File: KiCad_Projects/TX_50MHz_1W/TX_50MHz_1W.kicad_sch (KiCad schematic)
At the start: 7 parts

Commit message: Sync TX and RX schematic connectivity with target netlists
Repair the electrical connectivity of both single-sheet schematics so that a
netlist exported with kicad-cli 10 matches the connectivity described by
TX_50MHz_1W.net / RX_50MHz_SDR.net and the TX/RX schematic blueprints.

TX_50MHz_1W.kicad_sch
- Split the I2C bus: two coincident global labels (I2C_SDA + I2C_SCL on the
  same point at ESP32 IO11) had merged SDA and SCL into one net that also
  dragged in the BGS12PL6 CTRL/RF2 pins and the SPF5043Z RF input.  SDA now
  lands on IO8 and SCL on IO9 only.
- Removed the wire chain that shorted ESP32 IO8..IO11 together.
- 3V3 rail: every IC VDD sat on an island with just its decoupling cap.
  Labelled U1/U2/U3/U6/U7/U8 supply pins onto 3V3, and grounded the six
  decoupling caps that had a floating leg.
- PA drain: dropped the junction that tied Q1 drain onto the Si5351A CLK1
  wire.  TX_PATH is now Q1 drain + BGS12PL6 RF1 + RFC L2, with V_BATT feeding
  the drain through L2 as the blueprint specifies.  TELEM_LO (CLK1 -> LT5560
  LO+) is carried by labels instead of a wire crossing the drain node.
- Telemetry RX chain: BGS12PL6 RF2 -> SPF5043Z RFin (RX_PATH) and SPF5043Z
  RFout -> LT5560 IN+ (LNA_OUT) were open (wires stopped short of the pin).
- ADC: the 10.7MHz filter output ran to a wire end 4.5mm away from the MCU.
  FL1 OUT and ESP32 IO10 are now on ADC_IN.
- T/R control: BGS12PL6 CTRL and ESP32 IO11 are now on TR_SW_CTRL.
- Output LPF: the four shunt caps had GND on their series legs, which shorted
  the BGS12PL6 antenna port and the whole filter to ground.  GND moved to the
  free leg of each cap and the series path is now a proper 4C/3L low-pass
  from the switch ANT pin to the SMA.

RX_50MHz_SDR.kicad_sch
- Si5351A VDD was held on 3V3 only by a label sitting mid-wire; moved it to
  the open end of the stub, matching the SCL/SDA stubs next to it.
- Removed the duplicate XTAL_A label (two identical labels on one point
  cancel each other out in KiCad, so th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
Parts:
- removed FL?: 10.7MHz_Filter, symbol Kraft6M:10.7MHz_Filter
- removed Q?: 1W PA, symbol RD01MUS2
- removed U?: SPF5043Z, symbol Kraft6M:SPF5043Z
- removed U?: LT5560, symbol Kraft6M:LT5560
- removed U?: ESP32-S3, symbol ESP32-S3-WROOM-1
- removed U?: BGS12PL6, symbol Kraft6M:BGS12PL6
- removed U?: Si5351A, symbol Si5351A
- added C1: 10nF, Capacitor_SMD:C_0603_1608Metric, symbol Kraft6M:C_10nF_0603
- added C10, C11, C6, C7, C8, C9: 0.1uF, Capacitor_SMD:C_0603_1608Metric, symbol Kraft6M:C_0.1uF_0603
- added C2, C5: 120pF, Capacitor_SMD:C_0805_2012Metric, symbol Kraft6M:C_120pF_0805
- added C3, C4: 220pF, Capacitor_SMD:C_0805_2012Metric, symbol Kraft6M:C_220pF_0805
- added FL1: 10.7MHz Murata SFE, Filter:Ceramic_Filter_Murata_SFE, symbol Kraft6M:10.7MHz_Filter
- added J1: AIL Stick, Connector_JST:JST_XH_B3B-XH-A_1x03_P2.50mm_Vertical, symbol Kraft6M:JST_XH_3Pin
- added J10: I2C Exp / OLED, Connector_JST:JST_XH_B4B-XH-A_1x04_P2.50mm_Vertical, symbol Kraft6M:JST_XH_4Pin
- added J11: ANT, Connector_Coaxial:SMA_Amphenol_132289_EdgeMount, symbol Kraft6M:SMA_Edge
- added J2: ELE Stick, Connector_JST:JST_XH_B3B-XH-A_1x03_P2.50mm_Vertical, symbol Kraft6M:JST_XH_3Pin
- added J3: THR Stick, Connector_JST:JST_XH_B3B-XH-A_1x03_P2.50mm_Vertical, symbol Kraft6M:JST_XH_3Pin
- added J4: RUD Stick, Connector_JST:JST_XH_B3B-XH-A_1x03_P2.50mm_Vertical, symbol Kraft6M:JST_XH_3Pin
- added J5: AUX5, Connector_JST:JST_XH_B3B-XH-A_1x03_P2.50mm_Vertical, symbol Kraft6M:JST_XH_3Pin
- added J6: AUX6, Connector_JST:JST_XH_B3B-XH-A_1x03_P2.50mm_Vertical, symbol Kraft6M:JST_XH_3Pin
- added J7: AUX7, Connector_JST:JST_XH_B3B-XH-A_1x03_P2.50mm_Vertical, symbol Kraft6M:JST_XH_3Pin
- added J8: V_BATT In (XT30), Connector_JST:JST_XH_B2B-XH-A_1x02_P2.50mm_Vertical, symbol Kraft6M:JST_XH_2Pin
- added J9: 5V Logic In, Connector_JST:JST_XH_B2B-XH-A_1x02_P2.50mm_Vertical, symbol Kraft6M:JST_XH_2Pin
- added L1: 150nH, Inductor_SMD:L_0603_1608Metric, symbol Kraft6M:L_150nH_0603
- added L2: 1.0uH (RFC), Inductor_SMD:L_1206_3216Metric, symbol Kraft6M:L_1.0uH_1206
- added L3, L4, L5: 180nH, Inductor_SMD:L_0805_2012Metric, symbol Kraft6M:L_180nH_0805
- added Q1: RD01MUS2 (1W PA), Package_TO_SOT_SMD:SOT-89-3, symbol Kraft6M:RD01MUS2
- added U1: ESP32-S3-WROOM-1-N16R8, RF_Module:ESP32-S3-WROOM-1-N16R8, symbol Kraft6M:ESP32-S3-WROOM-1
- added U2: Si5351A-B-GT, Package_SO:MSOP-10_3x3mm_P0.5mm, symbol Kraft6M:Si5351A
- added U3: BGS12PL6 (T/R SW), Package_SON:TSLP-6-4_0.7x1.1mm_P0.4mm, symbol Kraft6M:BGS12PL6
- added U4: SPF5043Z (LNA), Package_TO_SOT_SMD:SOT-343_SC-70-4, symbol Kraft6M:SPF5043Z
- added U5: LT5560 (Mixer), Package_SON:DFN-8-1EP_2x2mm_P0.5mm_EP0.6x1.0mm, symbol Kraft6M:LT5560
- added U6: ADS1115IDGSR (0x48), Package_SO:VSSOP-10_3x3mm_P0.5mm, symbol Kraft6M:ADS1115
- added U7: ADS1115IDGSR (0x49), Package_SO:VSSOP-10_3x3mm_P0.5mm, symbol Kraft6M:ADS1115
- added U8: SH1106 1.3in OLED, Display:OLED-13-128x64, symbol Kraft6M:OLED_SH1106_I2C
- added Y1: 26.000MHz, Crystal:Crystal_SMD_3225-4Pin_3.2x2.5mm, symbol Kraft6M:Crystal_26MHz
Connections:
- new net: C3.2, L3.2, L4.1
- new net: U2.2 (XA), Y1.1
- new net: U2.3 (XB), Y1.2
- new net: L1.2, Q1.1 (G)
- new net: C1.1, U2.6 (CLK0)
- new net: C1.2, L1.1
- new net: FL1.1 (IN), U5.5 (OUT+)
- new net 3V3: C10.1, C10.2, C11.1, C11.2, C2.1, C3.1, C4.1, C5.1, C6.1, C6.2, C7.1, C7.2, C8.1, C8.2, C9.1, C9.2, FL1.2 (GND), J1.1 (P1), J1.2 (P2), J1.3 (P3), J10.1 (P1), J10.2 (P2), J11.2 (P2), J2.1 (P1), J2.3 (P3), J3.1 (P1), J3.3 (P3), J4.1 (P1), J4.2 (P2), J4.3 (P3), J5.1 (P1), J5.2 (P2), J5.3 (P3), J6.1 (P1), J6.3 (P3), J7.1 (P1), J7.2 (P2), J7.3 (P3), J8.2 (P2), J9.2 (P2), Q1.2 (S), U1.1 (GND), U1.2 (3V3), U1.3 (EN), U1.41 (GND), U2.1 (VDD), U2.10 (GND), U2.9 (VDDO), U3.2 (GND), U3.6 (VDD), U4.2 (GND), U4.4 (GND), U5.2 (IN-), U5.3 (EN), U5.4 (VCC), U5.6 (OUT-), U5.8 (LO-), U5.9 (GND), U6.1 (ADDR), U6.3 (GND), U6.4 (AIN0), U6.5 (AIN1), U6.8 (VDD), U7.1 (ADDR), U7.3 (GND), U7.4 (AIN0), U7.5 (AIN1), U7.8 (VDD), U8.1 (VCC), U8.2 (GND)
- new net 5V: J9.1 (P1)
- new net ADC_IN: FL1.3 (OUT), U1.13 (IO10)
- new net I2C_SCL: J10.3 (P3), U1.12 (IO9), U2.4 (SCL), U6.10 (SCL), U7.10 (SCL), U8.3 (SCL)
- new net I2C_SDA: J10.4 (P4), U1.11 (IO8), U2.5 (SDA), U6.9 (SDA), U7.9 (SDA), U8.4 (SDA)
- new net LNA_OUT: U4.3 (RFout), U5.1 (IN+)
- new net LPF_IN: C2.2, L3.1, U3.5 (ANT)
- new net LPF_N3: C4.2, L4.2, L5.1
- new net LPF_OUT: C5.2, J11.1 (P1), L5.2
- new net RX_PATH: U3.1 (RF2), U4.1 (RFin)
- new net TELEM_LO: U2.7 (CLK1), U5.7 (LO+)
- new net TR_SW_CTRL: U1.14 (IO11), U3.4 (CTRL)
- new net TX_PATH: L2.1, Q1.3 (D), U3.3 (RF1)
- new net VBATT_SENSE: U7.7 (AIN3)
- new net V_BATT: J8.1 (P1), L2.2
- no-connect marks 0 -> 3

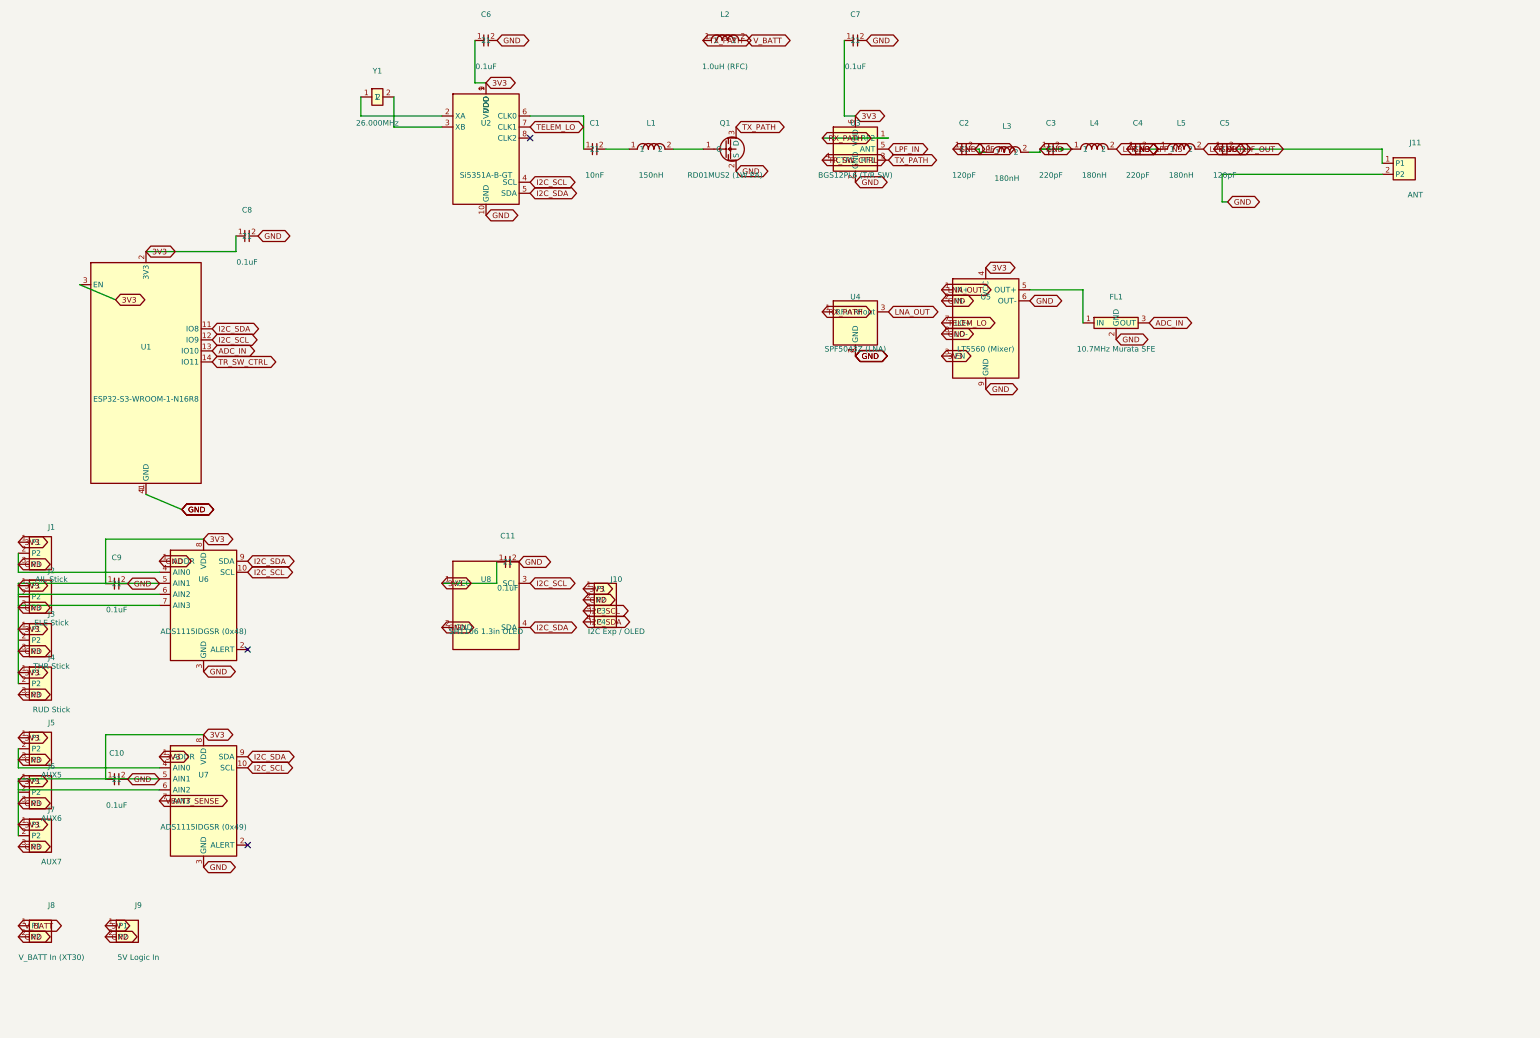
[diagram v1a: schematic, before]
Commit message: Lay out TX and RX schematics for readability (cosmetic only)
Both sheets had all content crammed into the top-left corner with
overlapping connector labels. Repositioned symbols into functional
bands with generous spacing:

TX (A3): three bands - TX RF chain (crystal -> Si5351 synth -> RD01MUS2
PA -> BGS12PL6 T/R switch -> 7-element LPF ladder -> ANT) across the
top with the LPF laid out as one straight line; RX down-conversion
chain plus OLED/I2C in the middle; ESP32, both ADS1115 + stick blocks
and the remaining stick/aux/power headers along the bottom. J1-J7 were
clipping the left page edge at x=2mm; now inset with real vertical
pitch between entries.

RX: page reduced A2 -> A3 (A2 was ~4x oversized for the content), then
five bands - RF signal path, RF support (clamps/bias/decoupling placed
under the IC each one serves), LO + ESP32 + servo outputs, 5V->3V3
power chain, and bulk cap + INA219 telemetry. Servo headers J5-J12
regrouped from one 18mm-pitch column (labels collided) into two
columns of four at 31mm pitch.

Connectivity is unchanged: symbols were translated only as whole rigid
groups (symbol plus every wire/label coincident with its pins), and
netlists exported before and after with kicad-cli compare as an
identical partition of (ref,pin) pairs into nets - TX 36 nets / 132
pins, RX 39 nets / 134 pins. No net, symbol, value or property was
added, removed or changed; the diff touches only coordinate values
plus RX's paper size.

Co-Authored-By: Claude Sonnet 5 <noreply@anthropic.com>
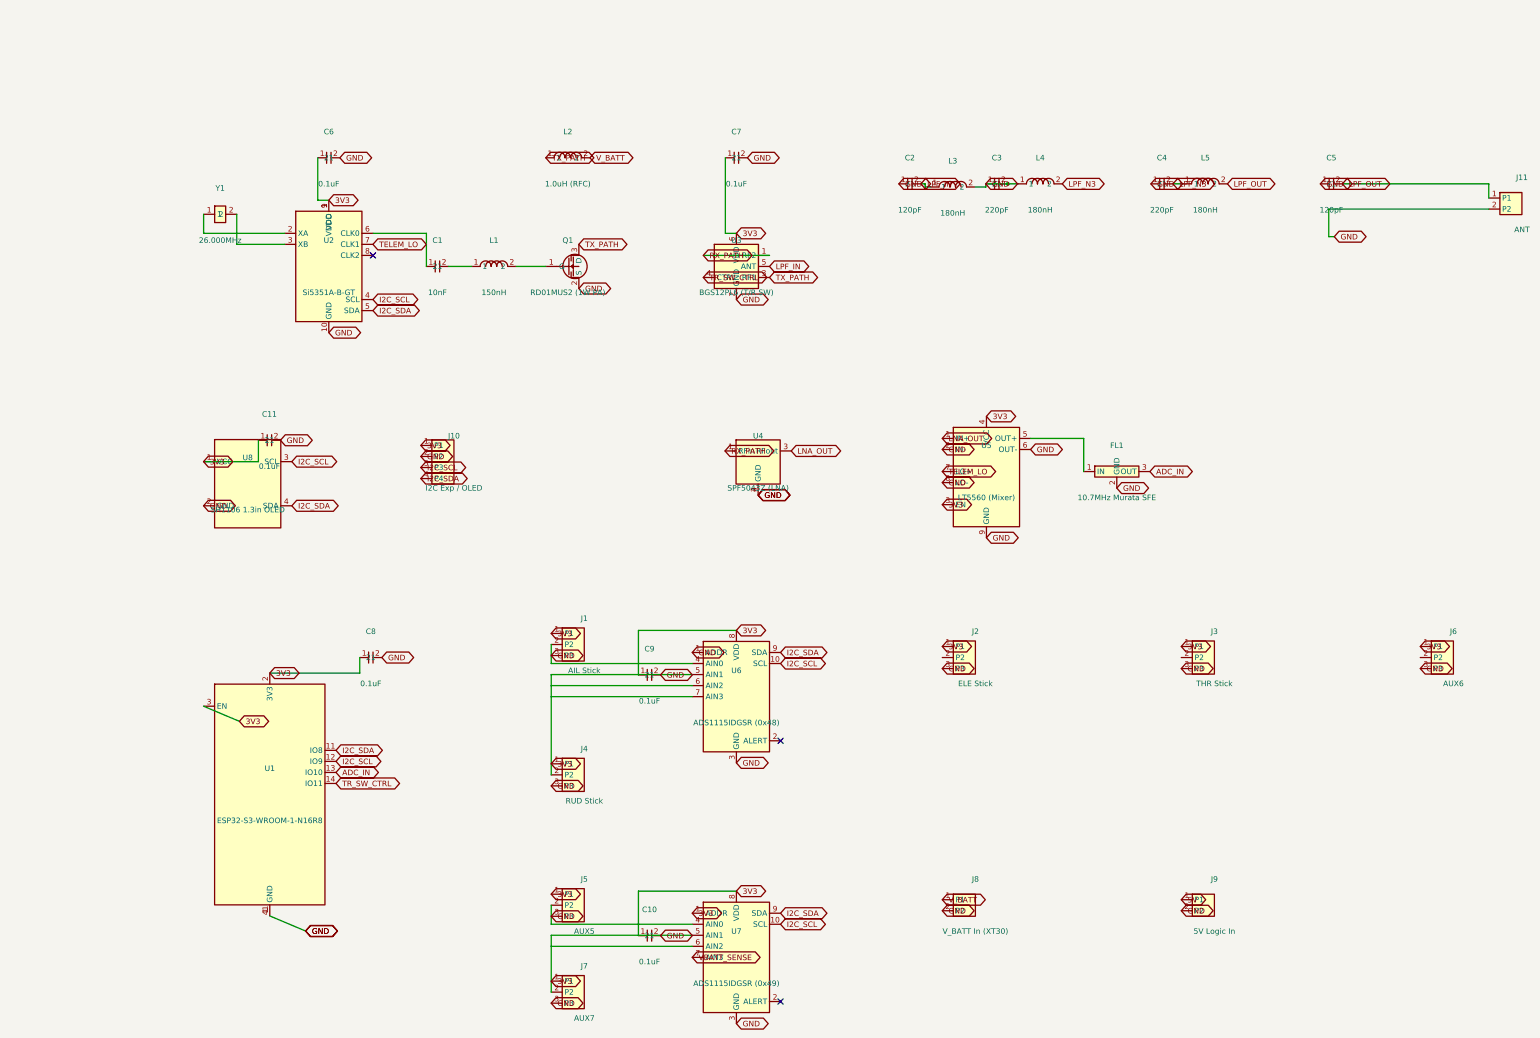
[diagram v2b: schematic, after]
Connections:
- net 3V3: no longer C10.2, C11.2, C2.1, C3.1, C4.1, C5.1, C6.2, C7.2, C8.2, C9.2, FL1.2 (GND), J1.2 (P2), J1.3 (P3), J10.2 (P2), J11.2 (P2), J2.3 (P3), J3.3 (P3), J4.3 (P3), J5.2 (P2), J5.3 (P3), J6.3 (P3), J7.3 (P3), J8.2 (P2), J9.2 (P2), Q1.2 (S), U1.1 (GND), U1.41 (GND), U2.10 (GND), U3.2 (GND), U4.2 (GND), U4.4 (GND), U5.2 (IN-), U5.6 (OUT-), U5.8 (LO-), U5.9 (GND), U6.1 (ADDR), U6.3 (GND), U6.4 (AIN0), U7.3 (GND), U7.4 (AIN0), U8.2 (GND)
- new net GND: C10.2, C11.2, C2.1, C3.1, C4.1, C5.1, C6.2, C7.2, C8.2, C9.2, FL1.2 (GND), J1.2 (P2), J1.3 (P3), J10.2 (P2), J11.2 (P2), J2.3 (P3), J3.3 (P3), J4.3 (P3), J5.2 (P2), J5.3 (P3), J6.3 (P3), J7.3 (P3), J8.2 (P2), J9.2 (P2), Q1.2 (S), U1.1 (GND), U1.41 (GND), U2.10 (GND), U3.2 (GND), U4.2 (GND), U4.4 (GND), U5.2 (IN-), U5.6 (OUT-), U5.8 (LO-), U5.9 (GND), U6.1 (ADDR), U6.3 (GND), U6.4 (AIN0), U7.3 (GND), U7.4 (AIN0), U8.2 (GND)
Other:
- moved on the sheet: C1, C10, C11, C2, C3, C4, C5, C6, C7, C8, C9, FL1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
